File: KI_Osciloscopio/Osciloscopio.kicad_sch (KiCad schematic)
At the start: 36 parts, among them J1 Barrel Jack, U1 MCP6004, U2 74HC4051, U3 LM7805, U4 LM1117-3.3

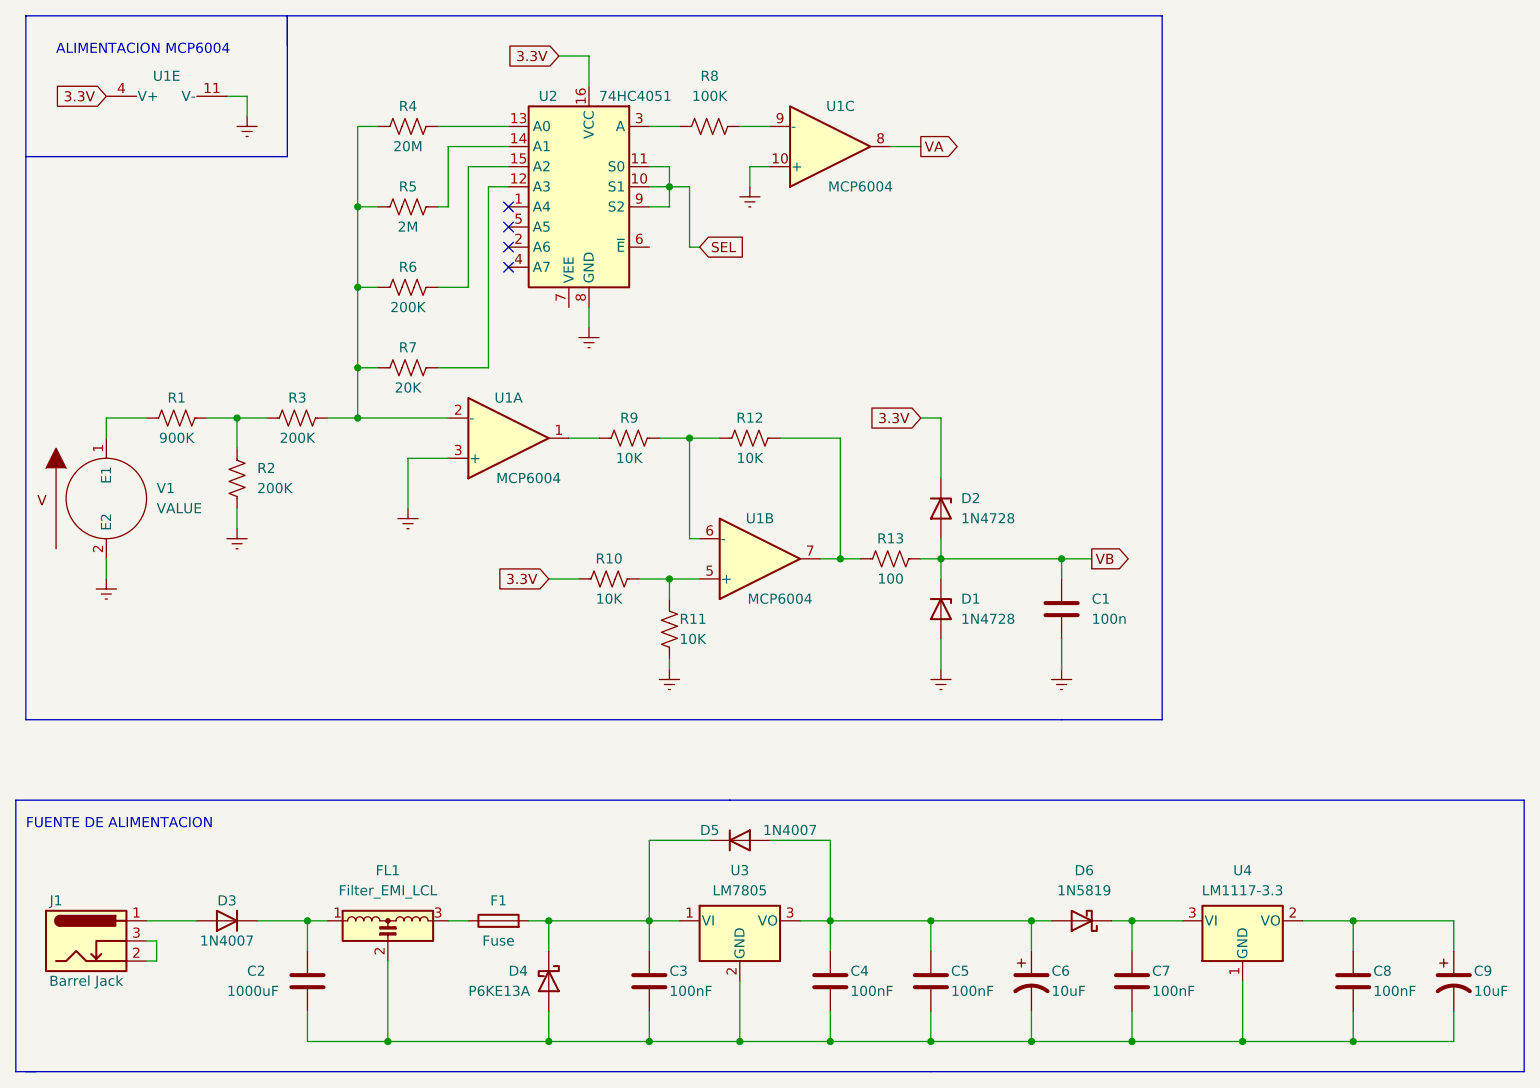
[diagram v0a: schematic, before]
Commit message: Incorporacion de un LPF Multiple Feedback
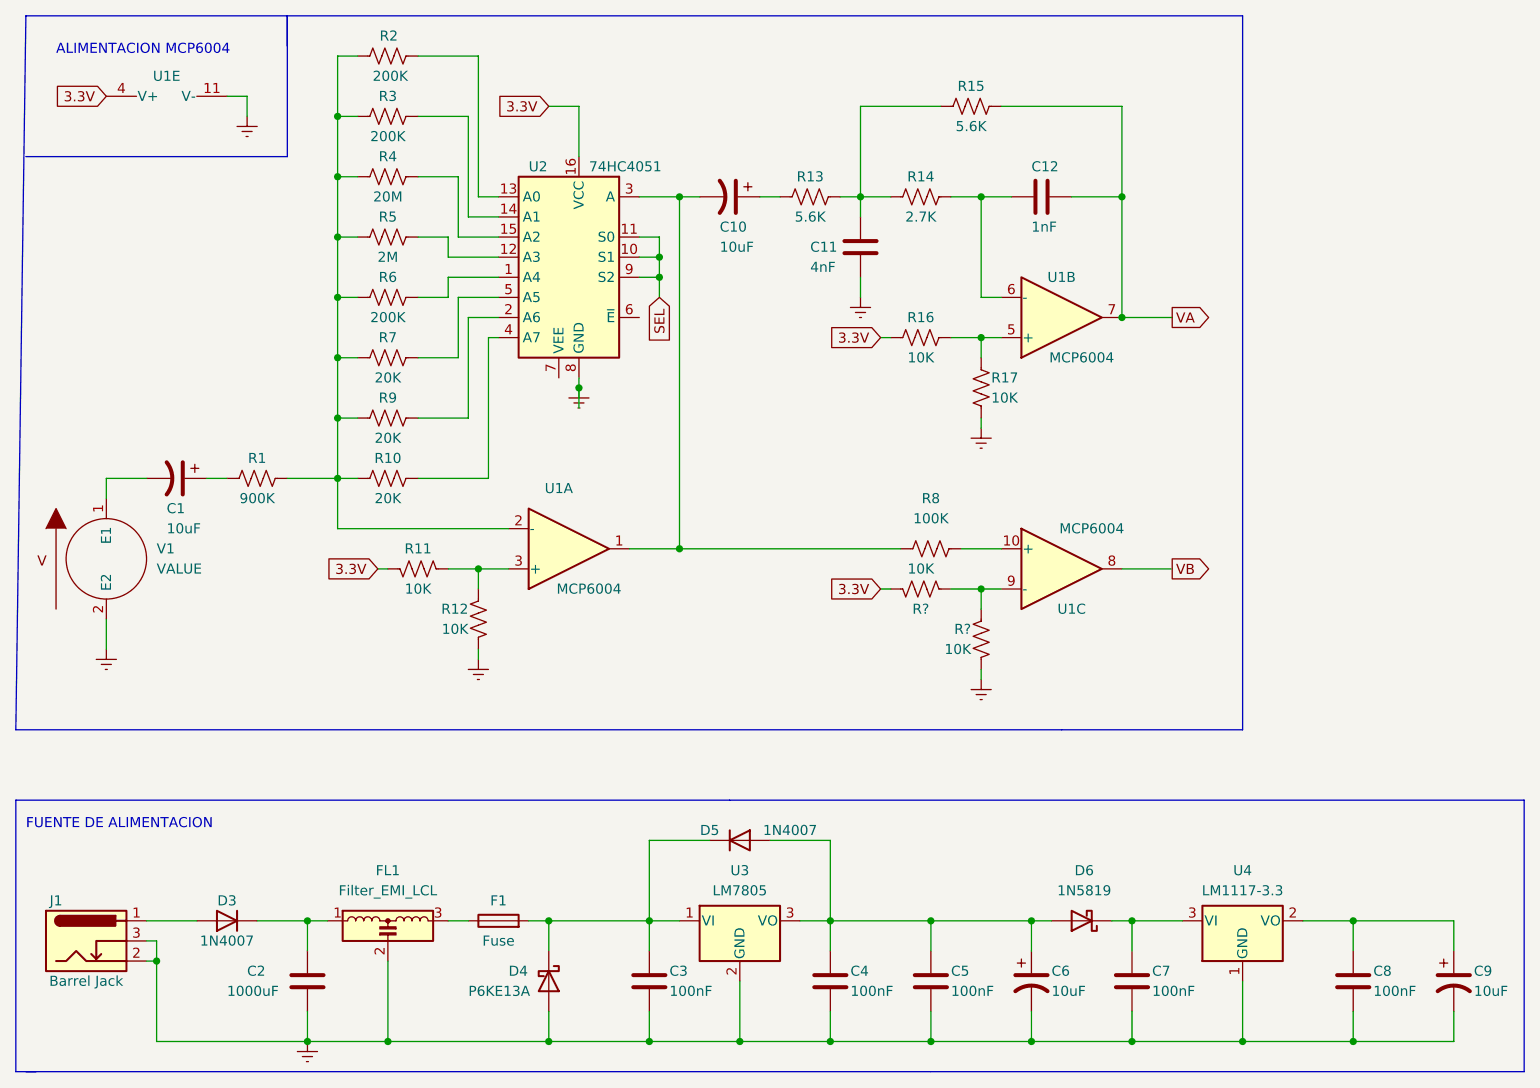
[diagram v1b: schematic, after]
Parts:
- removed C1: 100n, symbol Device:C
- removed D1, D2: 1N4728, symbol Device:D_Zener
- added C1, C10: 10uF, symbol Device:C_Polarized_US
- added C11: 4nF, symbol Device:C
- added C12: 1nF, symbol Device:C
- added R10, R9: 20K, symbol Device:R_US
- added R11, R? (x2): 10K, symbol Device:R_US
- added R15: 5.6K, symbol Device:R_US
- R13: value 100 -> 5.6K
- R14: renamed from R9; value 10K -> 2.7K
- renumbered R10 to R16, R11 to R17
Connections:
- net 3.3V: now also R11.2, R?.2
- net Earth: now also C2.2, C3.2, C4.2, C5.2, C6.2, C7.2, C8.2, C9.2, D4.2 (A), FL1.2, J1.2, J1.3, U3.2 (GND), U4.1 (GND)
- net GNDREF: now also R12.2, C11.1, R?.2; no longer R2.2, U1.10 (+), U1.3 (+)
- net VA: now also U1.7, C12.1, R15.1; no longer U1.8
- net VB: now also U1.8; no longer R13.2
- net at R5.1: now also U2.12 (A3); no longer U2.14 (A1)
- net at R4.2, R5.2, R6.2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: now also R1.1, R2.1, R3.2, R10.2, R9.2; no longer R3.1
- net at R14.1, U1.6 (-): now also C12.2; no longer R12.2
- net at R14.2: now also R13.1, C11.2, R15.2; no longer U1.1
- net at U2.13 (A0): now also R2.2; no longer R4.1
- net at U2.1 (A4): now also R6.1
- net at R7.1: now also U2.5 (A5); no longer U2.12 (A3)
- net at U2.15 (A2): now also R4.1; no longer R6.1
- net at U2.2 (A6): now also R9.1
- net at R8.2, U2.3 (A): now also U1.1, C10.2
- net at U2.4 (A7): now also R10.1
- net at U1.9 (-): now also R?.1, R?.1; no longer R8.1
- net at R1.2: now also C1.1; no longer V1.1 (E1)
- new net: R11.1, R12.1, U1.3 (+)
- new net: C10.1, R13.2
- new net: R3.1, U2.14 (A1)
- new net: C1.2, V1.1 (E1)
- new net: R8.1, U1.10 (+)
- no-connect marks 4 -> 0
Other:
- moved on the sheet: R1, R14, R16, R17, R2, R3, R4, R5, R6, R7, R8, U1A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

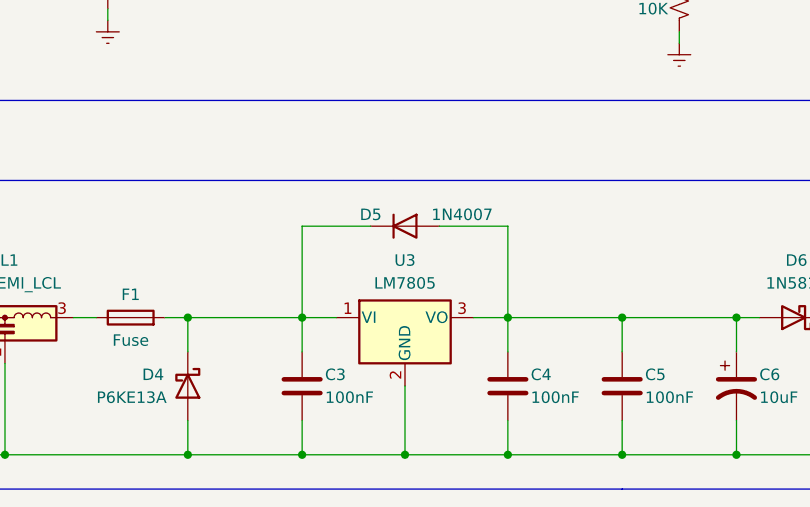
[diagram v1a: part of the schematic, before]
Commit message: Cambie regulador de tension 7805
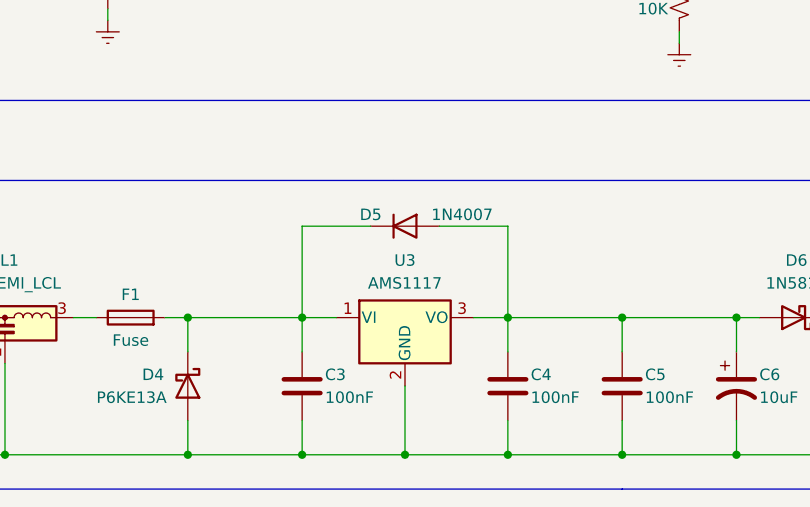
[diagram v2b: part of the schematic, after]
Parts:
- U3: value LM7805 -> AMS1117
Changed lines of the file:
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@@
     (in_bom yes) (on_board yes)
     (property "Reference" "U3" (id 0) (at 114.3 137.16 0))
-    (property "Value" "LM7805" (id 1) (at 114.3 139.7 0))
+    (property "Value" "AMS1117" (id 1) (at 114.3 139.7 0))
     (property "Footprint" "Package_TO_SOT_THT:TO-220-3_Vertical" (id 2) (at 114.3 137.795 0)
       (effects (font (size 1.27 1.27) italic) hide)
@@
     )
     (path "/02f4eb51-7294-4fca-9719-0ab752a1d6ed"
-      (reference "U3") (unit 1) (value "LM7805") (footprint "Package_TO_SOT_THT:TO-220-3_Vertical")
+      (reference "U3") (unit 1) (value "AMS1117") (footprint "Package_TO_SOT_THT:TO-220-3_Vertical")
     )
     (path "/3a131e3e-9f8a-40a2-8ed5-4e47ca92d0c5"
